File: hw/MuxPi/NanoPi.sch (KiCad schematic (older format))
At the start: 43 parts, among them IC2 ATTINY10-TS8R, P10 USB_OTG_MICRO_USB, P11 ZL262-20SG, P12 ZL201-04G, P13 PBTD16S, P14 ZL262-26DG, P15 PBTD16S, P16 UBA-4R-D14-4D, P18 CONN_02X03, Q12 BSO130P03S, Q8 2N7002, Q9 2N7002, U14 FT230XQ

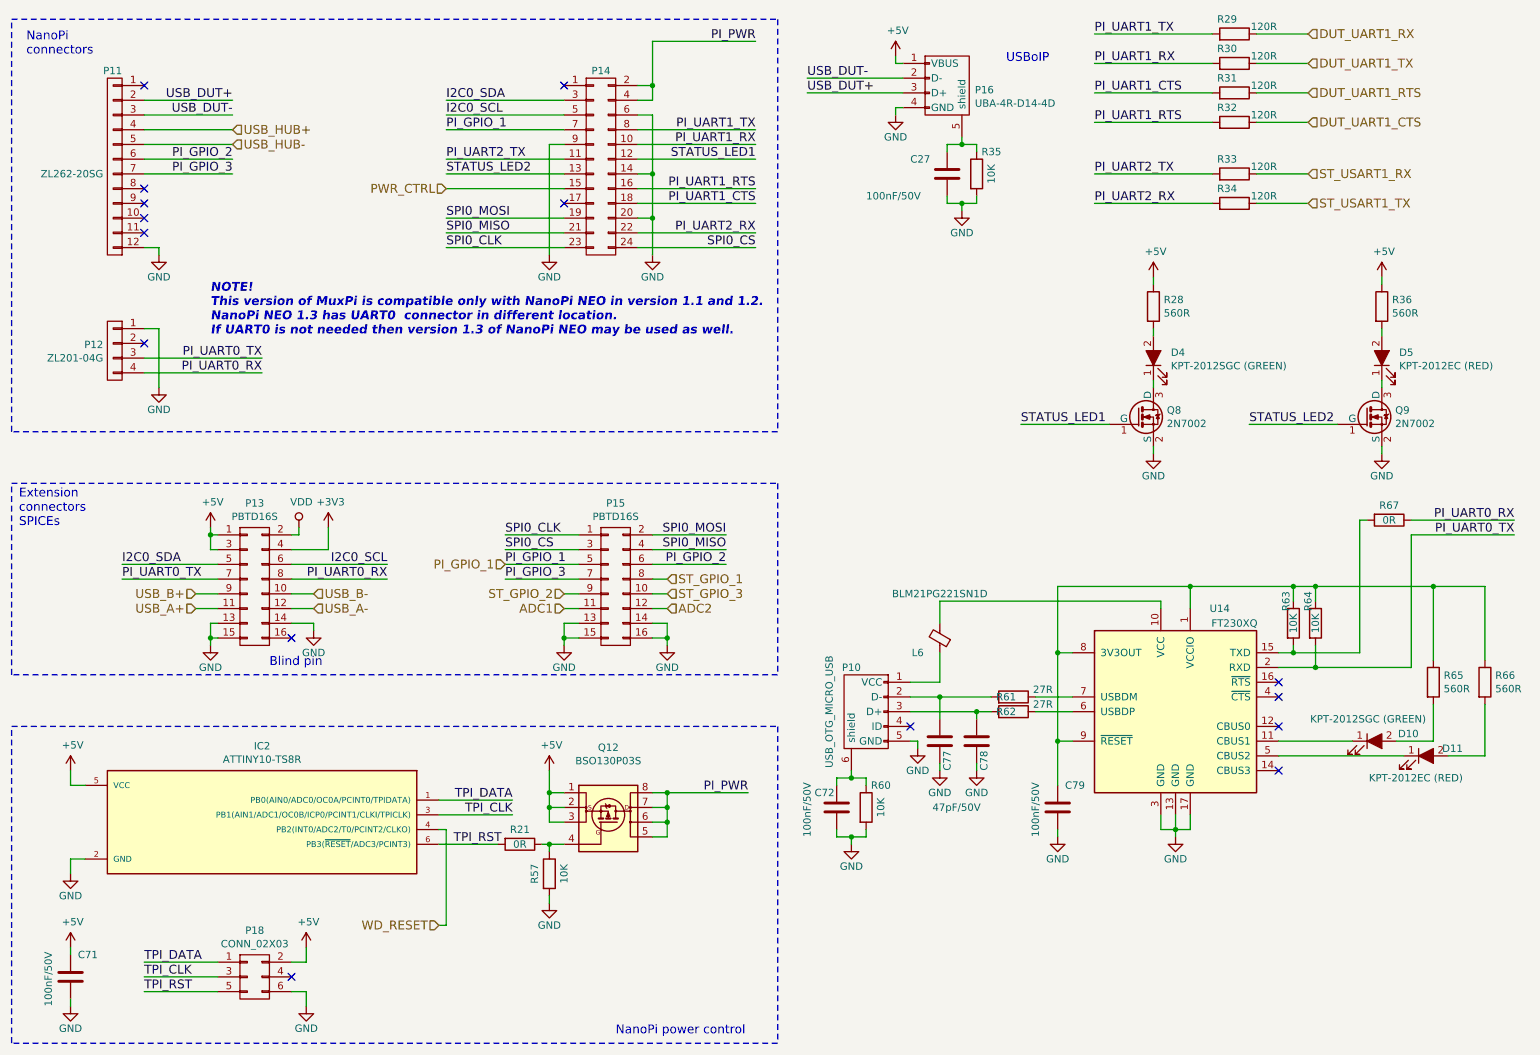
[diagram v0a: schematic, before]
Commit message: Add detailed info to MuxPi electronic components
The additional information includes manufacturer names and
manufacturer symbols for all components except ceramic capacitors
and resistors. It allows to create BOM (Bill Of Materials) with
actual product names.

Change-Id: Id1c518bba60322d4b8b132ad14261806070abc27
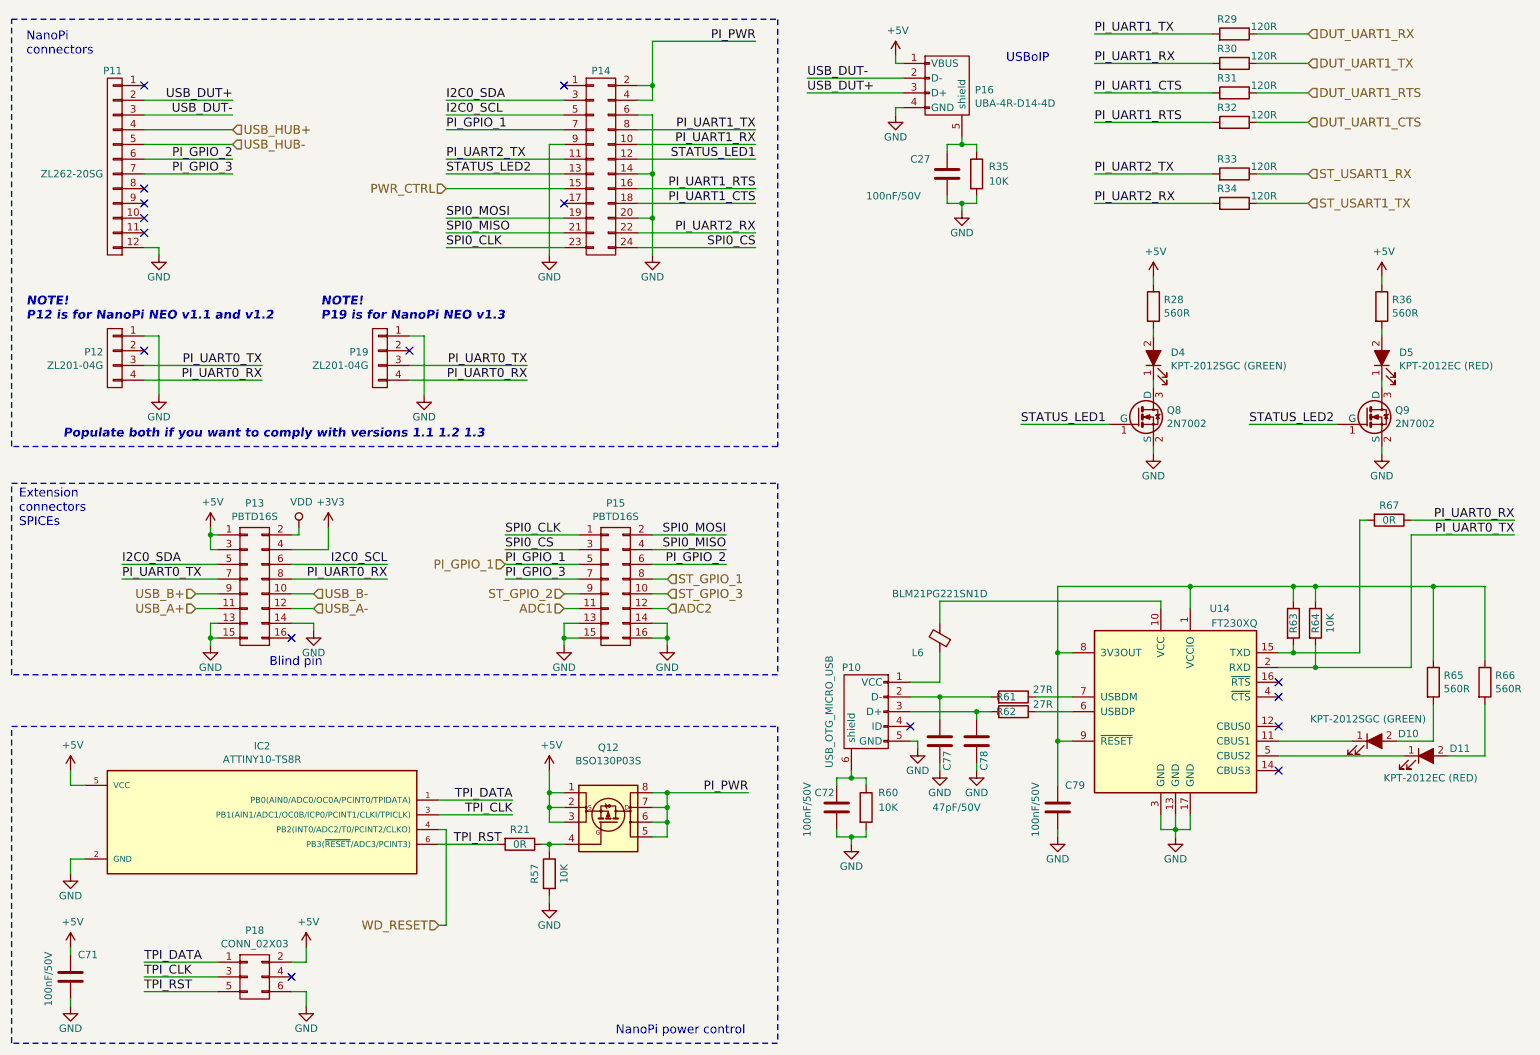
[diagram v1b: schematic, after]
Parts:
- added P19: ZL201-04G, mux-footprints:pin_strip_2.54_s_1x4, symbol MuxPi:CONN_01X04
- D10, D4: Manufacturer (none) -> KINGBRIGHT ELECTRONIC; Symbol (none) -> KPT-2012SGC
- D11, D5: Manufacturer (none) -> KINGBRIGHT ELECTRONIC; Symbol (none) -> KPT-2012EC
- IC2: Manufacturer (none) -> MICROCHIP (ATMEL); Symbol (none) -> ATTINY10-TS8R
- L6: Manufacturer (none) -> MURATA; Symbol (none) -> BLM21PG221SN1D
- P10: Manufacturer (none) -> MOLEX; Symbol (none) -> 1050170001
- P11: Complementary manufacturer (none) -> NINIGI; Complementary symbol (none) -> ZL2019-20; Manufacturer (none) -> CONNFLY; Note May be more than 1x12 pin. In that case we will crop. -> (none); Shop link http://www.tme.eu/pl/details/zl262-20sg/listwy-i-gniazda-ko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 -> https://www.tme.eu/pl/details/zl262-20sg/listwy-i-gniazda-k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; Symbol (none) -> DS1023-1*20S21
- P12: Complementary manufacturer (none) -> CONNFLY; Complementary shop link (none) -> http://www.tme.eu/pl/details/zl201-04g/listwy-i-gniazda-kol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; Complementary symbol (none) -> DS1021-1*4SF1-1; Manufacturer (none) -> CONNFLY; Shop link http://www.tme.eu/pl/details/zl201-04g/listwy-i-gniazda-kol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 -> https://www.tme.eu/pl/details/zl262-4sg/listwy-i-gniazda-ko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; Symbol (none) -> DS1023-1*4S21
- P13: Complementary device https://www.maritex.com.pl/zlacza/listwy_stykowe_kolkowe/li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 -> (none); Manufacturer (none) -> GREENCON; Symbol (none) -> PBTD16S
- P14: Complememntary symbol (none) -> ZL2019-40; Complementary manufacturer (none) -> NINIGI; Manufacturer (none) -> CONNFLY; Note May be more than 2x12 pin. In that case we will crop. -> (none); Shop link http://www.tme.eu/pl/details/zl262-26dg/listwy-i-gniazda-ko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 -> https://www.tme.eu/pl/details/zl262-26dg/listwy-i-gniazda-k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; Symbol (none) -> DS1023-2*13S21
- P15: Complementary device https://www.maritex.com.pl/zlacza/listwy_stykowe_kolkowe/li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 -> (none); Manufacturer (none) -> GREENCONN; Symbol (none) -> PBTD16S
- P16: Manufacturer (none) -> JST; Symbol (none) -> UBA-4R-D14-4D
- Q12: Manufacturer (none) -> INFINEON TECHNOLOGIES; Symbol (none) -> BSO130P03SHXUMA1
- Q8, Q9: Manufacturer (none) -> ON SEMICONDUCTOR (FAIRCHILD); Symbol (none) -> 2N7002
- R35, R60, R63, R64: Shop link (none) -> http://www.tme.eu/pl/details/rc0805jr-0710k/rezystory-smd-0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
- U14: Manufacturer (none) -> FTDI; Shop link (none) -> https://www.tme.eu/pl/details/ft230xq-t/uklady-scalone-inte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; Symbol (none) -> FT230XQ-T
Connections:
- net GND: now also P19.1 (P1)
- net PI_UART0_RX: now also P19.4 (P4)
- net PI_UART0_TX: now also P19.3 (P3)
- no-connect marks 15 -> 16
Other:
- note added: "NOTE!\nP12 is for NanoPi NEO v1.1 and v1.2"
- note added: "NOTE!\nP19 is for NanoPi NEO v1.3"
- note added: "Populate both if you want to comply with versions 1.1 1.2 1.3"
- note removed: "NOTE!\nThis version of MuxPi is compatible only with NanoPi NEO in version 1.1 and 1.2.\nNanoPi NEO 1.3 has UART0 connector in different location.\nIf UART0 is not needed then version 1.3 of NanoPi NEO may be used as well."
- moved on the sheet: P12

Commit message: Update hardware design to version 1.2
Change-Id: I36445887bfaa5fada88d8bf3915603605de47512
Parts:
- U14: footprint Housings_DFN_QFN:QFN-16-1EP_3x3mm_Pitch0.5mm -> Housings_DFN_QFN:QFN-16-1EP_4x4mm_Pitch0.65mm
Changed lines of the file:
@@
 EESchema Schematic File Version 4
+LIBS:MuxPi-cache
 EELAYER 26 0
 EELAYER END
@@
 encoding utf-8
 Sheet 8 12
-Title ""
-Date ""
-Rev ""
-Comp ""
-Comment1 ""
-Comment2 ""
+Title "MuxPi"
+Date "2018-04-20"
+Rev "1.2"
+Comp "SRPOL"
+Comment1 "Author: Adam Malinowski <a.malinowsk2@partner.samsung.com>"
+Comment2 "Copyright (c) 2016 - 2018 Samsung Electronics Co., Ltd All Rights Reserved"
 Comment3 ""
 Comment4 ""
@@
 F 0 "U14" H 9050 6050 50  0000 C CNN
 F 1 "FT230XQ" H 9150 5950 50  0000 C CNN
-F 2 "Housings_DFN_QFN:QFN-16-1EP_3x3mm_Pitch0.5mm" H 8750 5350 50  0001 C CNN
+F 2 "Housings_DFN_QFN:QFN-16-1EP_4x4mm_Pitch0.65mm" H 8750 5350 50  0001 C CNN
 F 3 "http://www.ftdichip.com/Products/ICs/FT230X.html" H 8750 5350 50  0001 C CNN
 F 4 "https://www.tme.eu/pl/details/ft230xq-t/uklady-scalone-interfejs-usb/ftdi/" H 8750 5350 50  0001 C CNN "Shop link"

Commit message: Update hardware design to version 1.3
Change-Id: I17b3f32943a6fd048f05d1b0d8676607dc54b976
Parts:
- added D12: BAR43CFILM, TO_SOT_Packages_SMD:SOT-23, symbol MuxPi:BAR43CFILM
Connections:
- net +5V: now also D12.1 (A)
- net at U14.10 (VCC): now also D12.3 (K); no longer L6.2
- new net: D12.2 (A), L6.2
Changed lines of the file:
@@
 Sheet 8 12
 Title "MuxPi"
-Date "2018-04-20"
-Rev "1.2"
+Date "2018-08-14"
+Rev "1.3"
 Comp "SRPOL"
 Comment1 "Author: Adam Malinowski <a.malinowsk2@partner.samsung.com>"
-Comment2 "Copyright (c) 2016 - 2018 Samsung Electronics Co., Ltd All Rights Reserved"
+Comment2 "Copyright (c) 2016 -2018 Samsung Electronics Co., Ltd All Rights Reserved"
 Comment3 ""
 Comment4 ""
@@
 Wire Wire Line
 	8750 6200 8750 6150
-Wire Wire Line
-	8650 4600 8650 4650
 $Comp
 L MuxPi:R R61
@@
 Wire Wire Line
 	7150 5150 7150 4950
-Wire Wire Line
-	7150 4750 7150 4600
-Wire Wire Line
-	7150 4600 8650 4600
 Wire Wire Line
 	6450 6150 6450 6200
@@
 	1    0    0    -1
 $EndComp
+Wire Wire Line
+	8650 4130 7710 4130
+Wire Wire Line
+	8650 4130 8650 4650
+$Comp
+L MuxPi:BAR43CFILM D12
+U 1 1 5B759F3D
+P 7460 4030
+F 0 "D12" H 7410 3814 50  0000 C CNN
+F 1 "BAR43CFILM" H 7410 3905 50  0000 C CNN
+F 2 "TO_SOT_Packages_SMD:SOT-23" H 7310 3830 50  0001 C CNN
+F 3 "www.st.com/resource/en/datasheet/bar42.pdf" H 7460 4030 50  0001 C CNN
+	1    7460 4030
+	-1   0    0    1
+$EndComp
+Wire Wire Line
+	7310 4230 7150 4230
+Wire Wire Line
+	7150 4230 7150 4750
+$Comp
+L MuxPi:+5V #PWR0210
+U 1 1 5B76899A
+P 7150 3960
+F 0 "#PWR0210" H 7150 3810 50  0001 C CNN
+F 1 "+5V" H 7165 4133 50  0000 C CNN
+F 2 "" H 7150 3960 50  0000 C CNN
+F 3 "" H 7150 3960 50  0000 C CNN
+	1    7150 3960
+	1    0    0    -1
+$EndComp
+Wire Wire Line
+	7150 3960 7150 4030
+Wire Wire Line
+	7150 4030 7310 4030
 $EndSCHEMATC
